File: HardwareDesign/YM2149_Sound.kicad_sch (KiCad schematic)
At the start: 20 parts, among them J801 Conn_01x02, J802 Conn_02x09_Odd_Even, J803 SJ1-3525N, U801 YM2149, U802 74HCT02, U803 74HCT04, U804 4 MHz

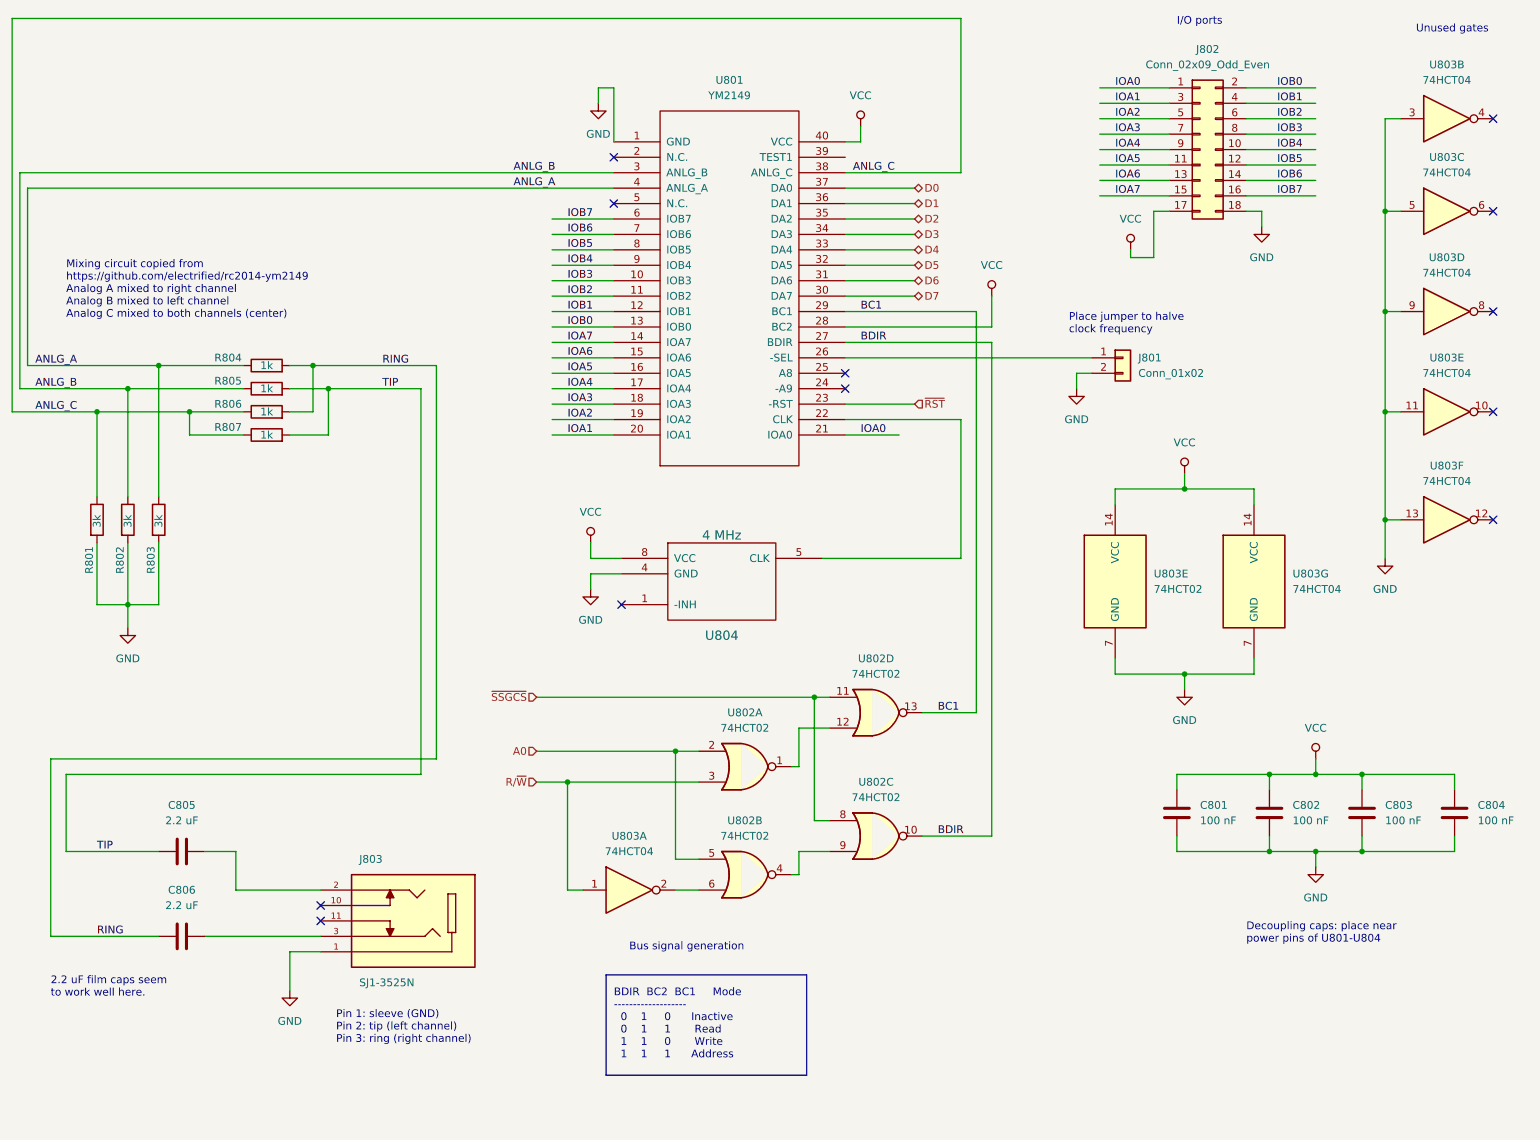
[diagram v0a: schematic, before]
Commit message: lots of changes to TMS9918A and YM2149 modules
Changed the TMS9918A circuit to use -RMEM and -WMEM rather than R/-W,
since -RMEM and -WMEM are properly synchronized with E and the overall
CPU bus cycle. (Duh!)

Also chnaged the YM2149 circuit to use -RMEM and -WMEM. However,
it's less clear that this is a desirable change, because we would
like BDIR and BC1 to change "at the same time", and only when
the chip is being accessed. However, if the chip select is asserted
before -RMEM/-WMEM are asserted, then meaningless BDIR and BC1
values are going to be generated, which is not good. Need to think
about this.
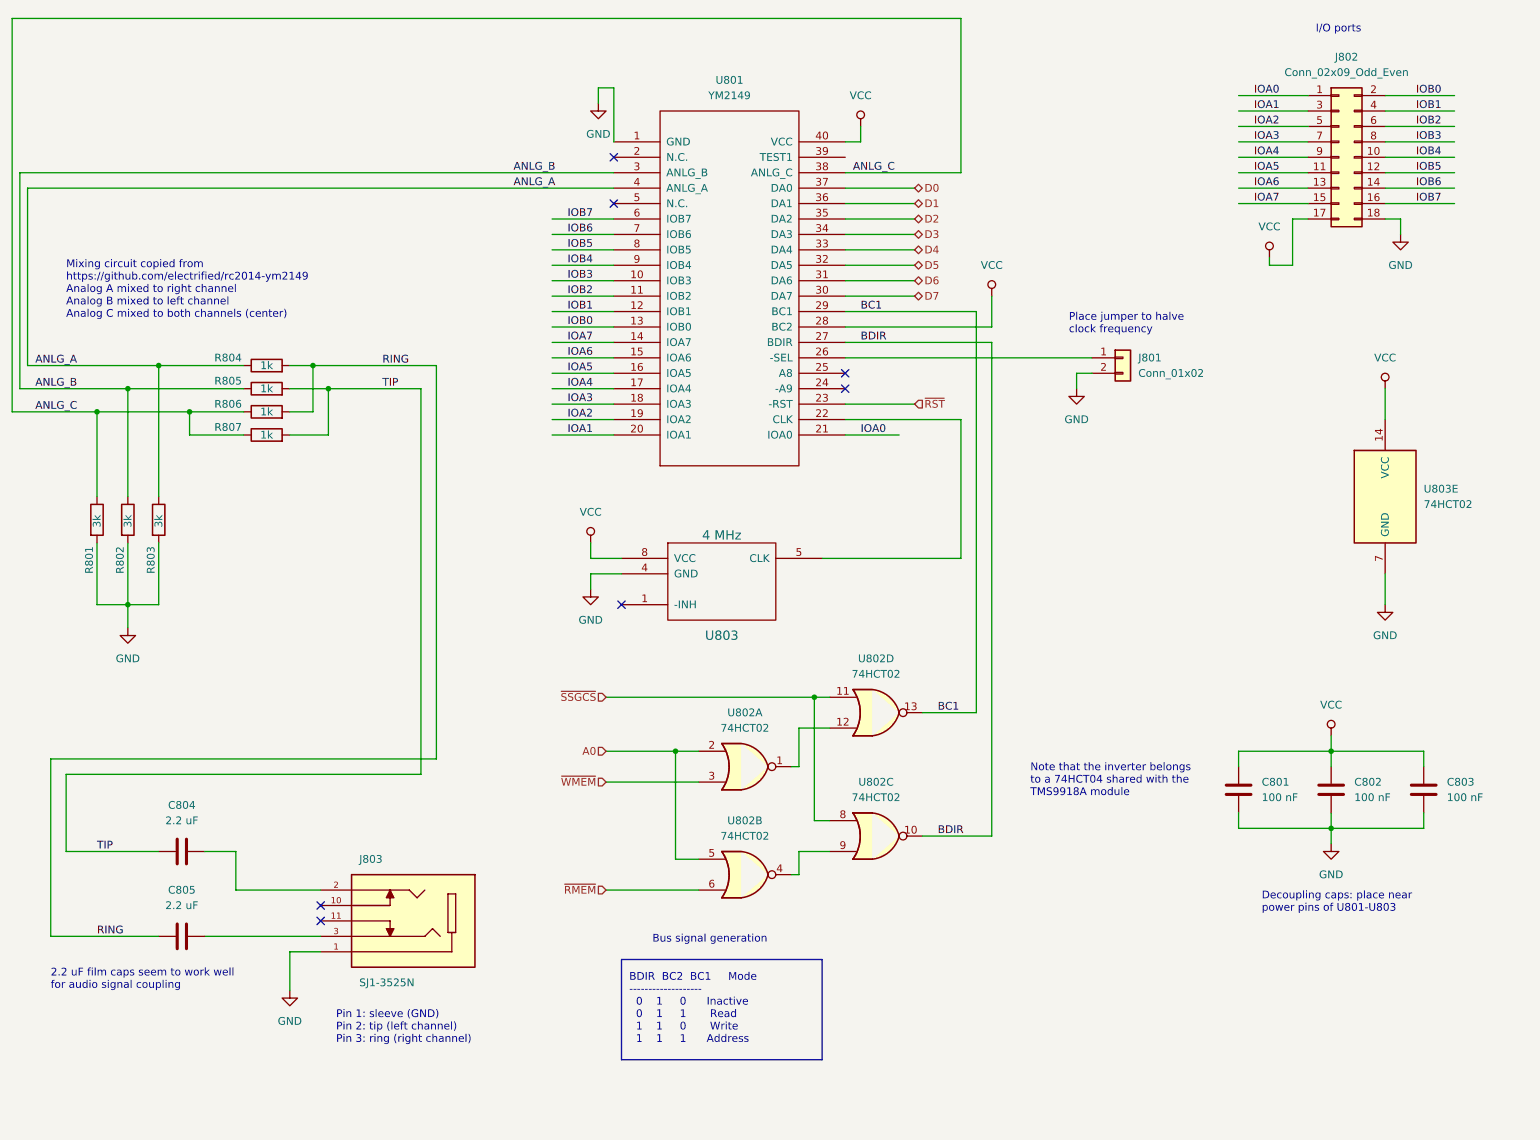
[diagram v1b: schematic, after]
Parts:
- removed C803: 100 nF, symbol device:C
- removed unit 3 of U803
- removed unit 6 of U803
- removed unit 4 of U803
- removed unit 1 of U803
- removed unit 7 of U803
- removed unit 2 of U803
- renumbered C804 to C803, C805 to C804, C806 to C805, U804 to U803
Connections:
- net ~{RMEM}: now reaches U802.6
- net R/~{W} renamed ~{WMEM}
- no-connect marks 12 -> 7
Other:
- note added: "2.2 uF film caps seem to work well for audio signal coupling"
- note added: "Decoupling caps: place near power pins of U801-U803"
- note added: "Note that the inverter belongs to a 74HCT04 shared with the TMS9918A module"
- note removed: "2.2 uF film caps seem to work well here."
- note removed: "Decoupling caps: place near power pins of U801-U804"
- note removed: "Unused gates"
- moved on the sheet: C801, C802, C803, J802, U803E

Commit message: reimplemented bus signal generation for YM2149
The changes should help ensure that BC1 and BDIR only
change from the inactive state when the chip is being
accessed (for a read or write.)
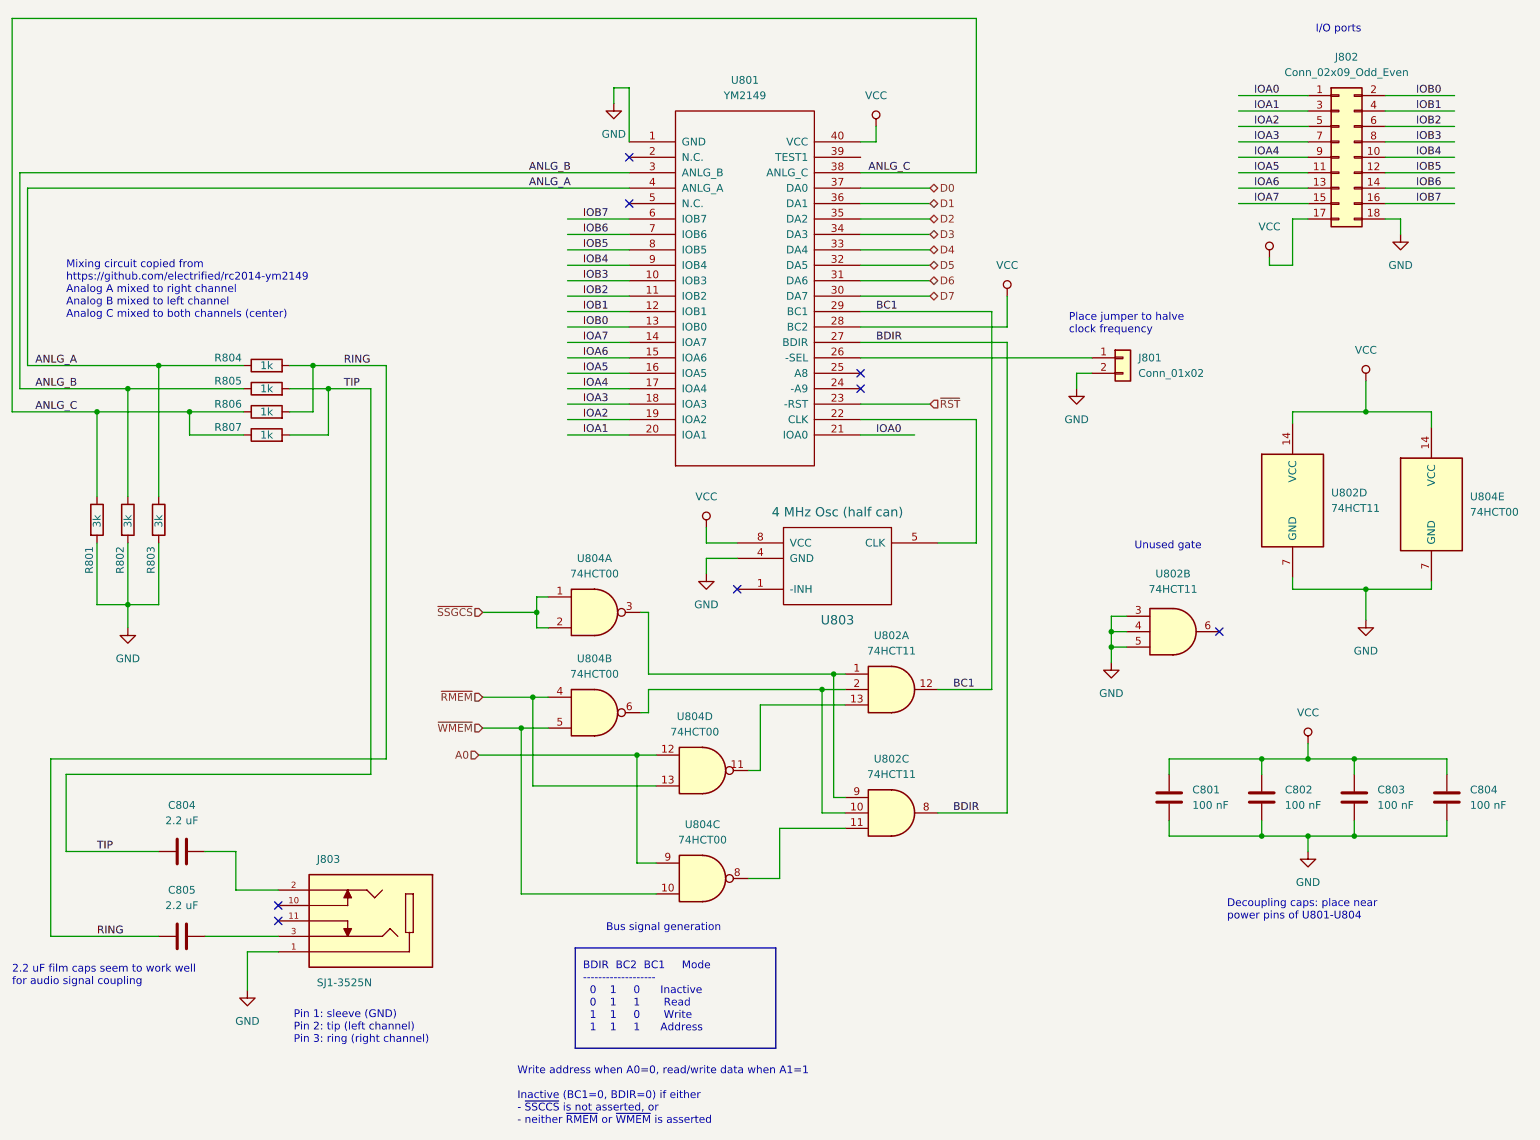
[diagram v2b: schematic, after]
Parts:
- removed U802: 74HCT02, symbol 74xx:74HCT02
- removed unit 5 of U803
- added C804: 100 nF, symbol device:C
- added U802: 74HCT11, symbol 74xx:74LS11
- added U804: 74HCT00, symbol 74xx:74HCT00
- U803: value 4 MHz -> 4 MHz Osc (half can)
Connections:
- net A0: now also U804.12, U804.9
- net BC1: now also U802.12
- net BDIR: now also U802.8
- net GND: now also C804.2, U802.3, U802.4, U802.5, U802.7 (GND), U804.7 (GND)
- net VCC: now also C804.1, U802.14 (VCC), U804.14 (VCC)
- net ~{RMEM}: now also U804.13, U804.4
- net ~{SSGCS}: now also U804.1, U804.2
- net ~{WMEM}: now also U804.10, U804.5
- new net: U802.13, U804.11
- new net: U802.10, U802.2, U804.6
- new net: U802.11, U804.8
- new net: U802.1, U802.9, U804.3
- no-connect marks 7 -> 8
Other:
- note added: "Decoupling caps: place near power pins of U801-U804"
- note added: "Unused gate"
- note added: "Write address when A0=0, read/write data when A1=1 Inactive (BC1=0, BDIR=0) if either - ~{SSCCS} is not asserted, or - neither ~{RMEM} or ~{WMEM} is asserted"
- note removed: "Decoupling caps: place near power pins of U801-U803"
- note removed: "Note that the inverter belongs to a 74HCT04 shared with the TMS9918A module"
- moved on the sheet: C801, C802, C803, J803, U801, U803

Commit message: fix typo
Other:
- note added: "Write address when A0=0, read/write data when A0=1 Inactive (BC1=0, BDIR=0) if either - ~{SSCCS} is not asserted, or - neither ~{RMEM} or ~{WMEM} is asserted"
- note removed: "Write address when A0=0, read/write data when A1=1 Inactive (BC1=0, BDIR=0) if either - ~{SSCCS} is not asserted, or - neither ~{RMEM} or ~{WMEM} is asserted"
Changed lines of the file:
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@@
     (effects (font (size 1.27 1.27)) (justify left bottom))
   )
-  (text "Write address when A0=0, read/write data when A1=1\n\nInactive (BC1=0, BDIR=0) if either\n- ~{SSCCS} is not asserted, or\n- neither ~{RMEM} or ~{WMEM} is asserted"
+  (text "Write address when A0=0, read/write data when A0=1\n\nInactive (BC1=0, BDIR=0) if either\n- ~{SSCCS} is not asserted, or\n- neither ~{RMEM} or ~{WMEM} is asserted"
     (at 99.695 200.025 0)
     (effects (font (size 1.27 1.27)) (justify left bottom))

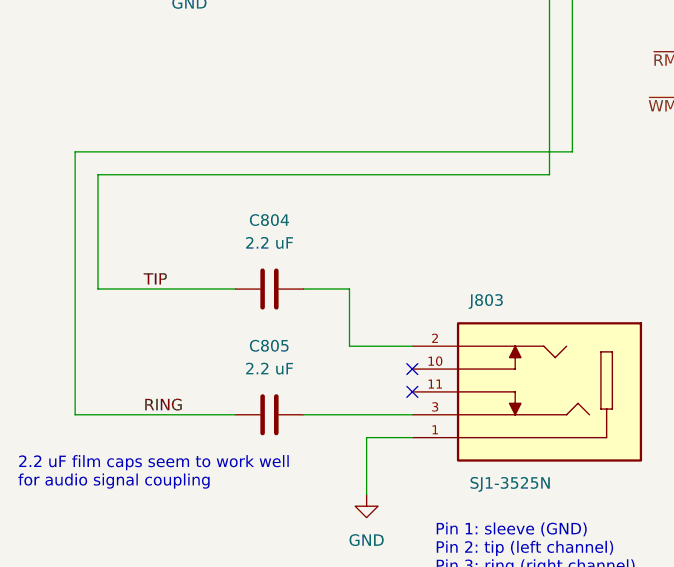
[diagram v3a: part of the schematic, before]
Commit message: footprint assignments for TMS9918A/YM2149 modules
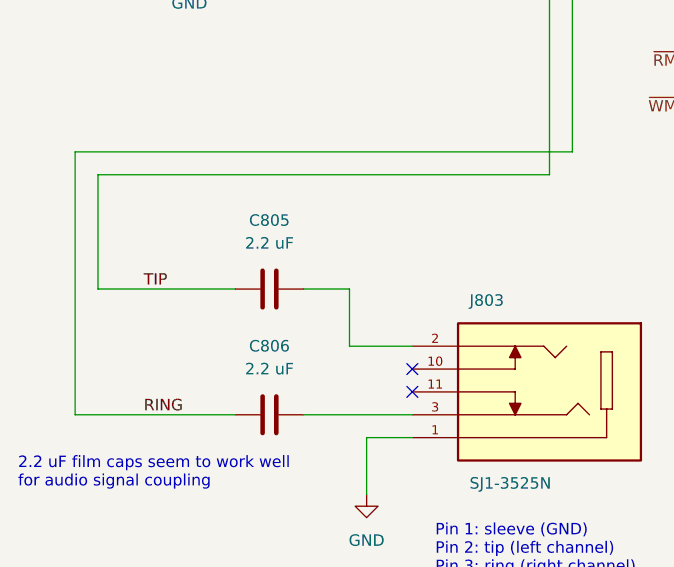
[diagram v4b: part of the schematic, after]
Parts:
- C801, C802, C803, C804: footprint (none) -> Capacitor_THT:C_Disc_D3.4mm_W2.1mm_P2.50mm
- C805: renamed from C804; footprint (none) -> Capacitor_THT:C_Rect_L7.0mm_W4.5mm_P5.00mm
- C806: renamed from C805; footprint (none) -> Capacitor_THT:C_Rect_L7.0mm_W4.5mm_P5.00mm
- J801: footprint (none) -> Connector_PinHeader_2.54mm:PinHeader_1x02_P2.54mm_Vertical
- J802: footprint (none) -> Connector_PinHeader_2.54mm:PinHeader_2x09_P2.54mm_Vertical
- R801, R802, R803, R804, R805, R806, R807: footprint (none) -> Resistor_THT:R_Axial_DIN0207_L6.3mm_D2.5mm_P7.62mm_Horizontal
- U801: footprint MODULE -> Package_DIP:DIP-40_W15.24mm_Socket
- U802, U804: footprint (none) -> Package_DIP:DIP-14_W7.62mm_Socket
- U803: footprint (none) -> Package_DIP:DIP-8_W7.62mm_Socket

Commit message: fix some footprint assignments
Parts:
- J803: footprint CUI_SJ1-3525N -> CUI_SJ1-3525N:CUI_SJ1-3525N
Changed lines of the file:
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@@
       (effects (font (size 1.27 1.27)) (justify right))
     )
-    (property "Footprint" "CUI_SJ1-3525N" (id 2) (at 75.565 166.37 0)
+    (property "Footprint" "CUI_SJ1-3525N:CUI_SJ1-3525N" (id 2) (at 75.565 166.37 0)
       (effects (font (size 1.27 1.27)) (justify bottom) hide)
     )

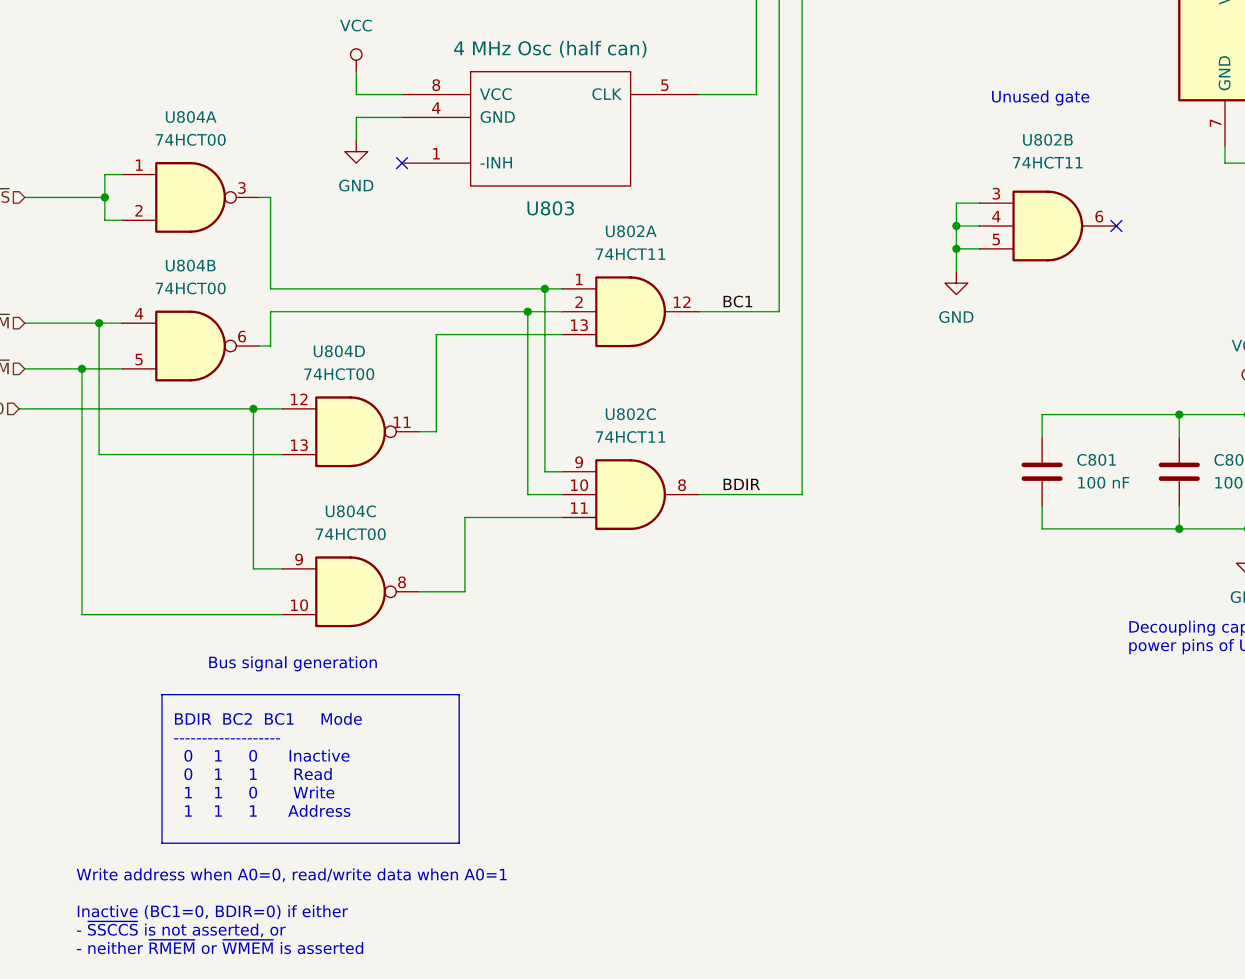
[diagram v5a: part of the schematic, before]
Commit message: initial schematic for FPGA display controller
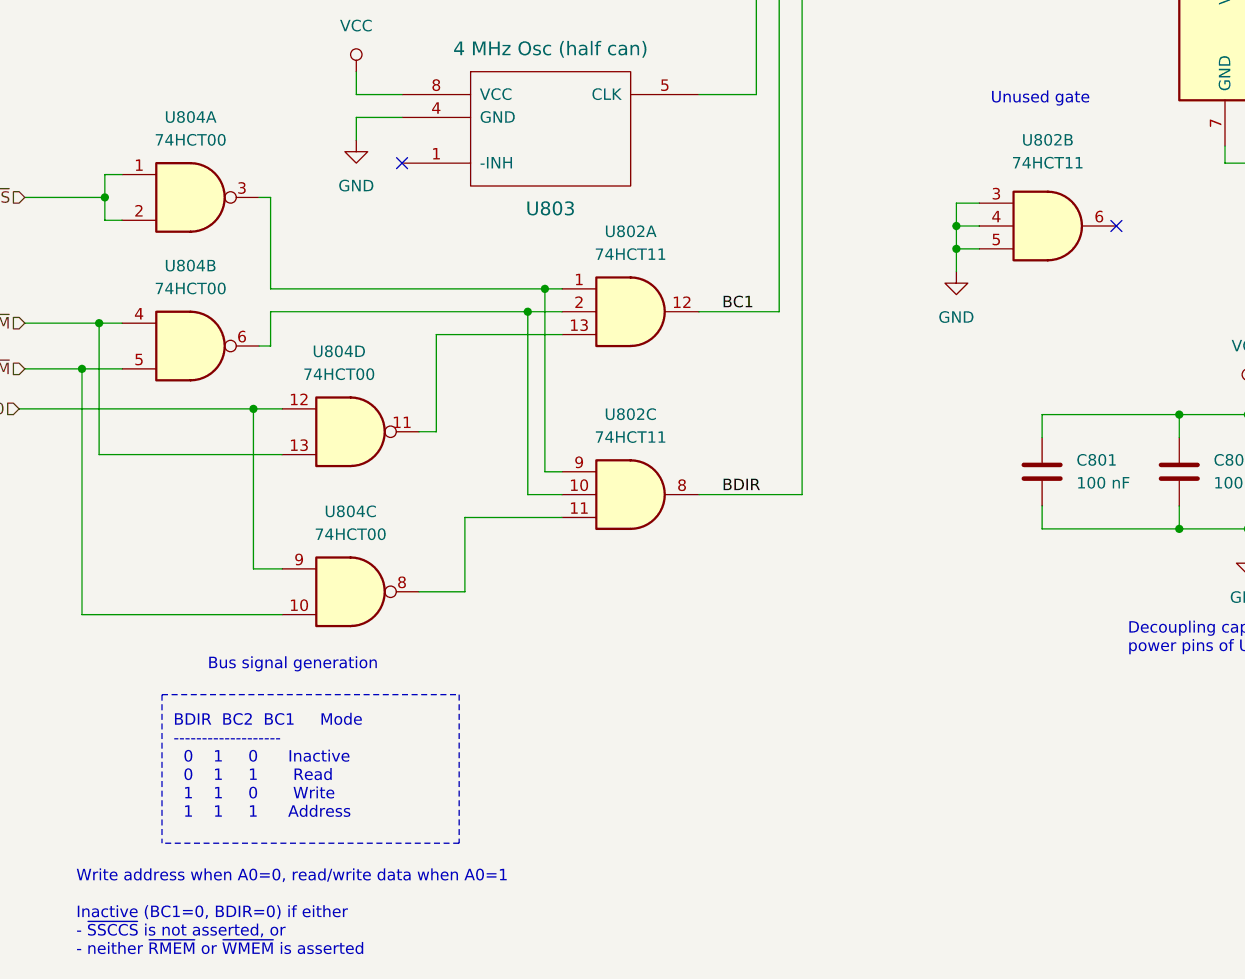
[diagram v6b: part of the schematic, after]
